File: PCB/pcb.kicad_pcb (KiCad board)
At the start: 2 copper layers, 61.9 x 61.9 mm, 9 parts, among them SW1 SW_Push, SW2 SW_Push, SW3 SW_Push, SW4 SW_Push, SW5 SW_Push, SW6 SW_Push, U1 XIAO-RP2040-DIP

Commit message: Changed from SK6812 to SK6812MINI-E
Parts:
- D1, D2: value SK6812 -> SK6812MINI-E
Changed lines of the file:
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@@
 			)
 		)
-		(property "Value" "SK6812"
+		(property "Value" "SK6812MINI-E"
 			(at 0 3.25 0)
 			(layer "F.Fab")
@@
 			)
 		)
-		(property "Value" "SK6812"
+		(property "Value" "SK6812MINI-E"
 			(at 0 3.25 0)
 			(layer "F.Fab")

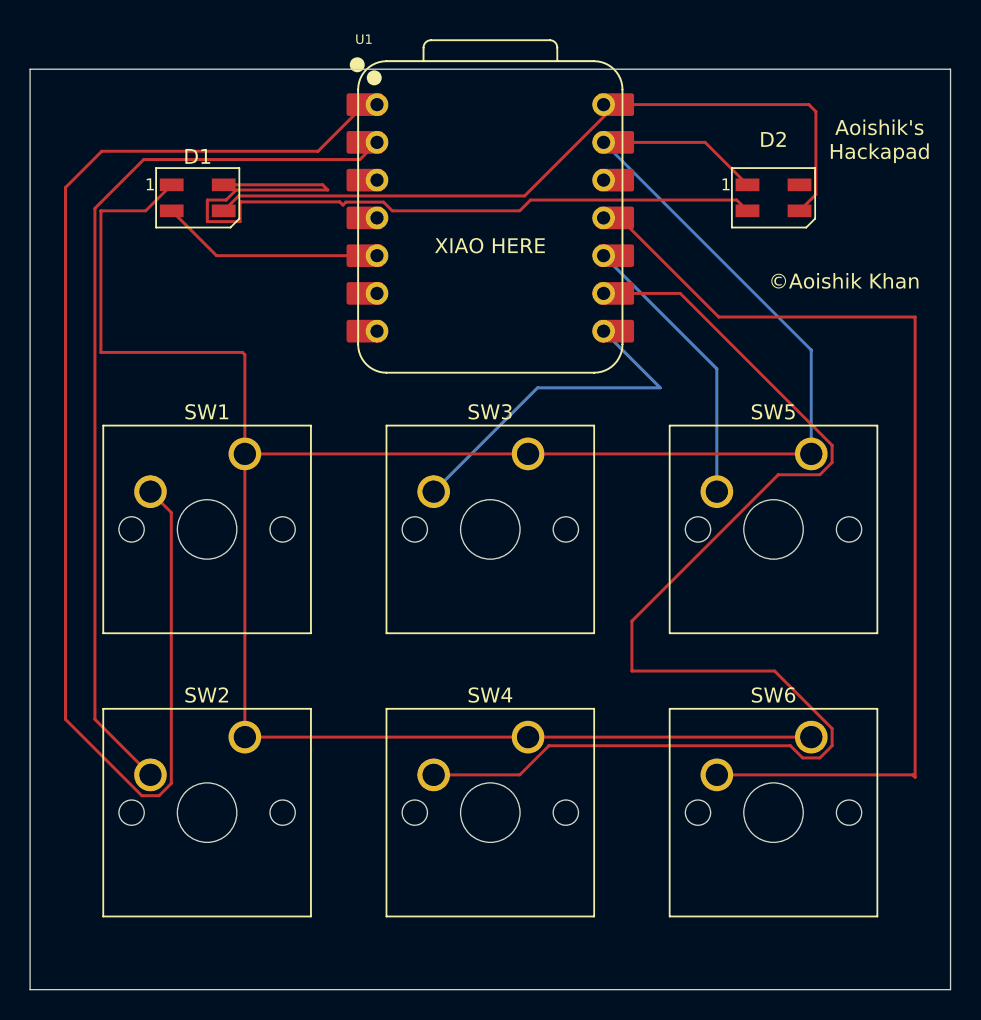
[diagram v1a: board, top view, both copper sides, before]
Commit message: Changed LEDs
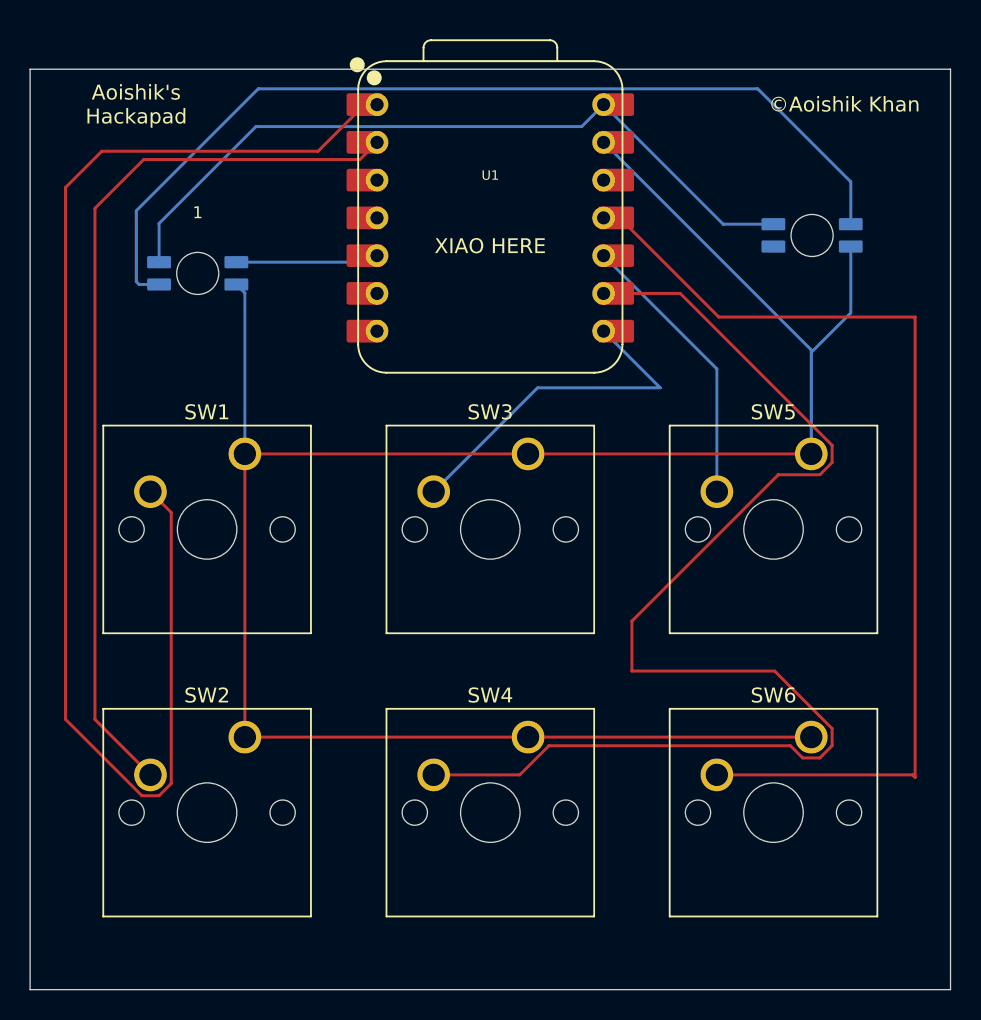
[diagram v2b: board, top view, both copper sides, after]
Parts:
- D1, D2: footprint LED_SMD:LED_SK6812MINI_PLCC4_3.5x3.5mm_P1.75mm -> HACKCLUB:MX_SK6812MINI-E_REV
- moved D2 3.64 mm to (174.0, 44.2)
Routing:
- net GND: track 163.4 -> 142.2 mm
- net Net-(D1-DOUT): track 55.6 -> 63.3 mm
- net Net-(D1-DIN): track 14.2 -> 9.64 mm
